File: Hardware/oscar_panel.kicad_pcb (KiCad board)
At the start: 2 copper layers, 71 x 128.5 mm, 11 parts

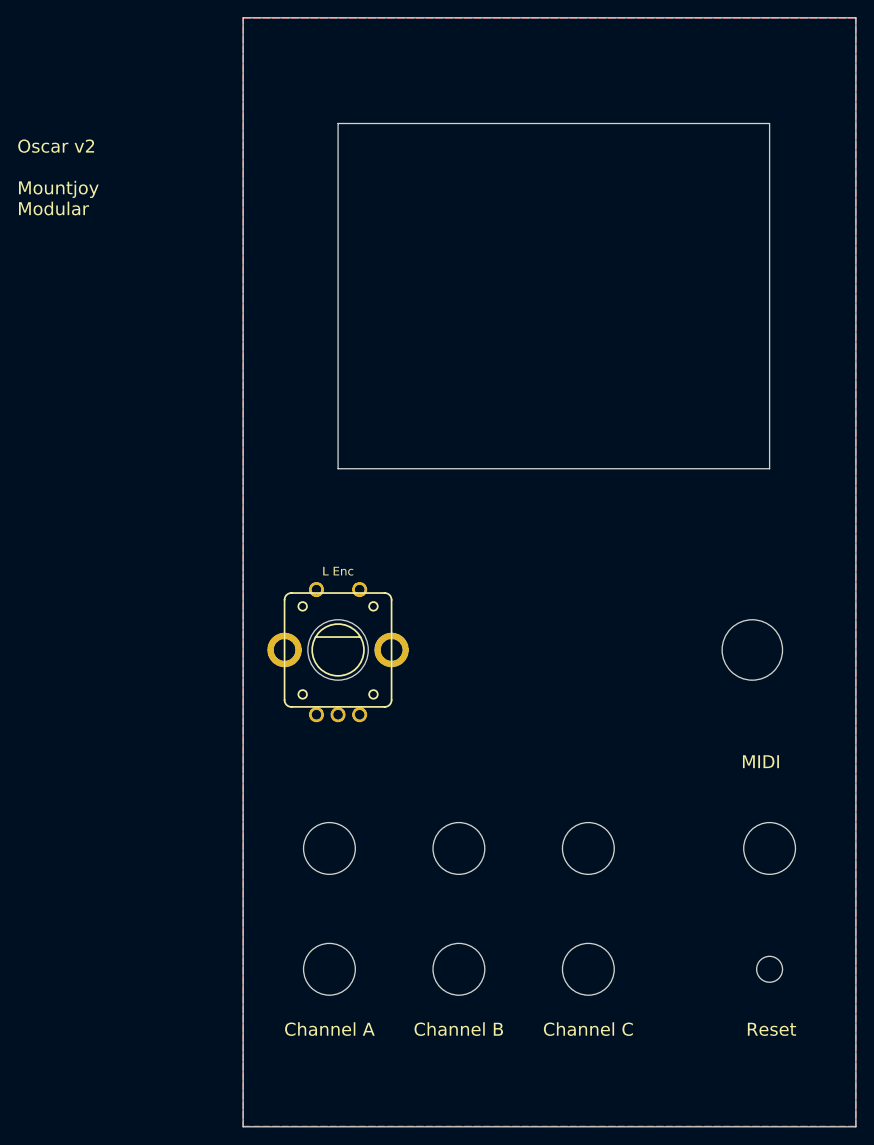
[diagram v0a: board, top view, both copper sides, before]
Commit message: Reorganised and relocated reposistory
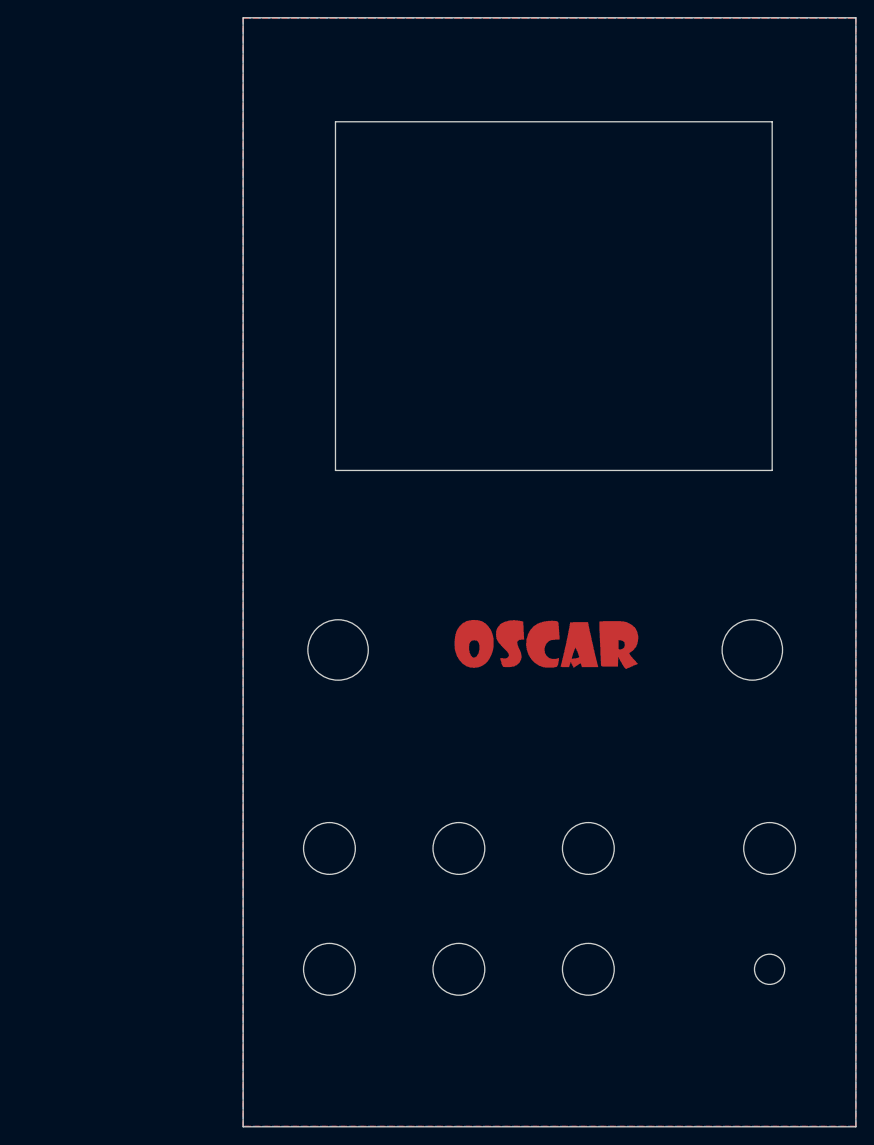
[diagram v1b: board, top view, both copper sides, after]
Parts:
- removed L Enc: Left_Encoder, Custom_Footprints:Encoder
- removed the Ref** at (186.0, 151.0)
- added G***: LOGO, oscar_logo:oscar_logo, F.Cu at (150.3, 113.7)
- added Ref**: Subminiature_Switch, Custom_Footprints:Sub_Miniature_Switch_MountingHole_3.5mm, F.Cu at (186.0, 151.0)
- added Ref**: Oval_Mounting_Hole, Custom_Footprints:Oval_Mounting_Hole, F.Cu at (188.5, 166.2)
- added Ref**: Oval_Mounting_Hole, Custom_Footprints:Oval_Mounting_Hole, F.Cu at (132.5, 166.2)
- added Ref**: Oval_Mounting_Hole, Custom_Footprints:Oval_Mounting_Hole, F.Cu at (188.5, 43.8)
- added Ref**: Oval_Mounting_Hole, Custom_Footprints:Oval_Mounting_Hole, F.Cu at (132.5, 43.8)
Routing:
- added copper zone on B.Cu, net (none)
- added copper zone on F.Cu, net (none)
- removed copper zone on B.Cu, net GND
- removed copper zone on F.Cu, net GND
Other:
- outline, holes or cut-outs redrawn
- board text added: "A"
- board text added: "B"
- board text added: "C"
- board text added: "In"
- board text added: "JLCJLCJLCJLC"
- board text added: "Menu"
- board text added: "Mode"
- board text added: "Mountjoy Modular"
- board text added: "OSCAR Panel v2"
- board text added: "Out"
- board text removed: "Channel A"
- board text removed: "Channel B"
- board text removed: "Channel C"
- board text removed: "Oscar v2 Mountjoy Modular"
